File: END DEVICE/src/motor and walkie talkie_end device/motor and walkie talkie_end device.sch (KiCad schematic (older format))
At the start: 28 parts, among them J1 ICSP, J2 FTDI_CONN, SW1 SW_Push, SW2 SW_Push, SW3 SW_Push, SW4 SW_Push, SW5 SW_Push, U1 ATmega328P-MU, Y1 Crystal

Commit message: second commit: updated schematic symbol(oscillator)
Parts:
- Y1: value Crystal -> 8MHz
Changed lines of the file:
@@
 P 5200 2900
 F 0 "Y1" V 5154 3031 50  0000 L CNN
-F 1 "Crystal" V 5245 3031 50  0000 L CNN
+F 1 "8MHz" V 5245 3031 50  0000 L CNN
 F 2 "" H 5200 2900 50  0001 C CNN
 F 3 "~" H 5200 2900 50  0001 C CNN

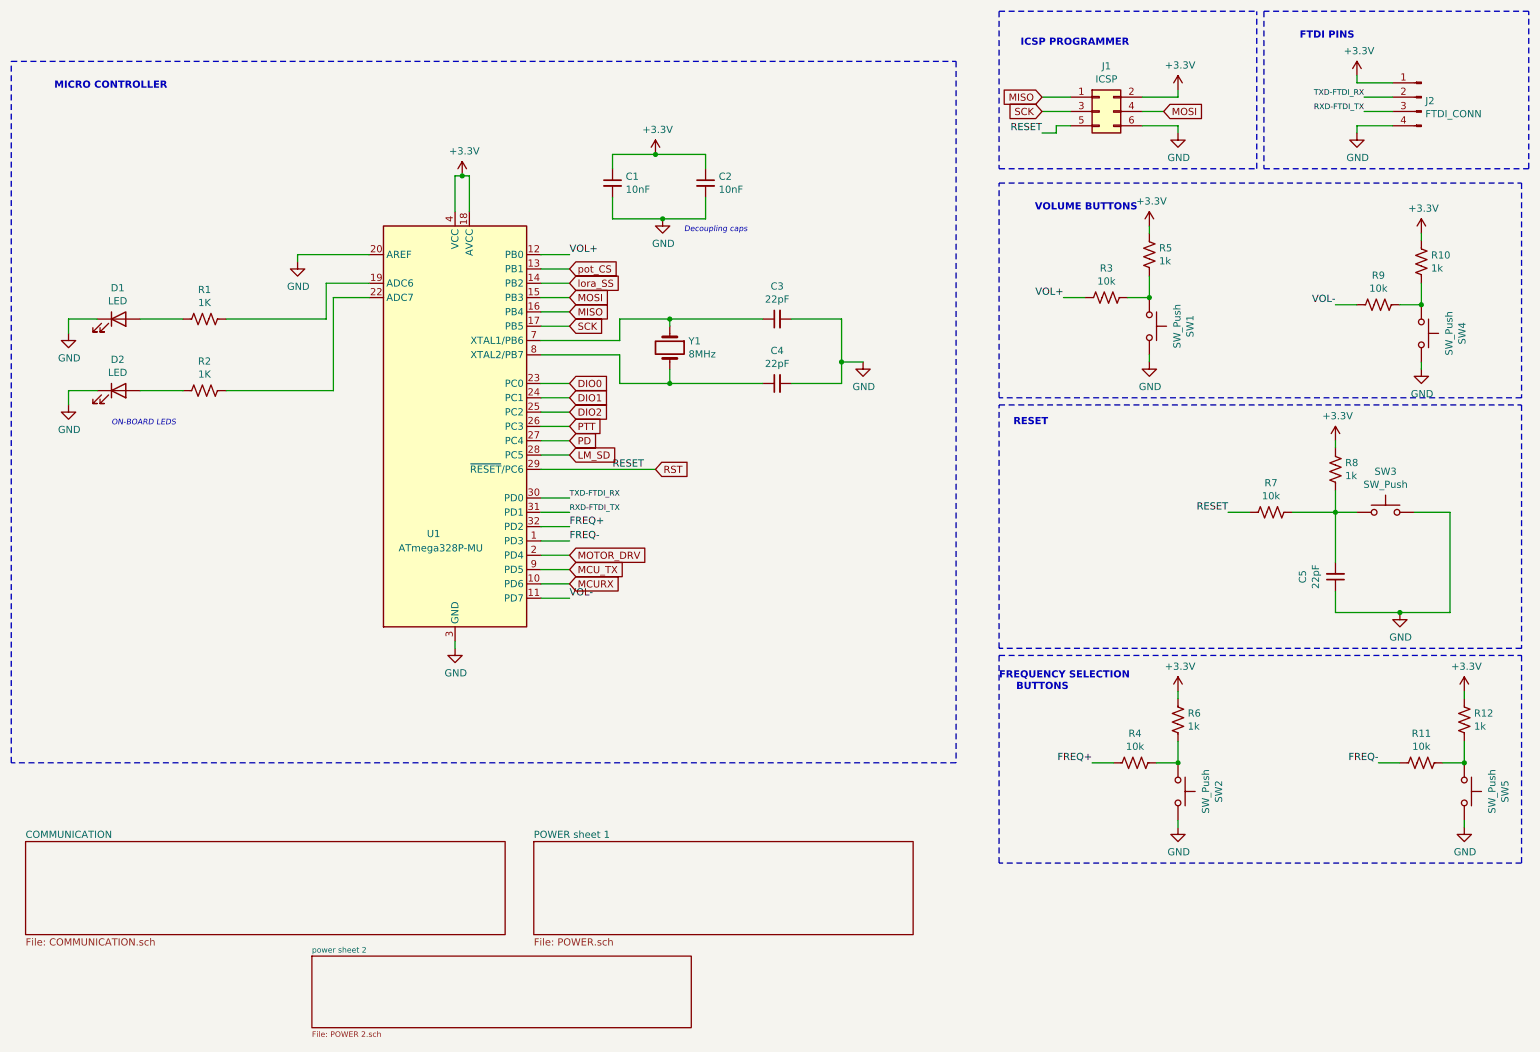
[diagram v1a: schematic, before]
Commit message: All footprint associations updated
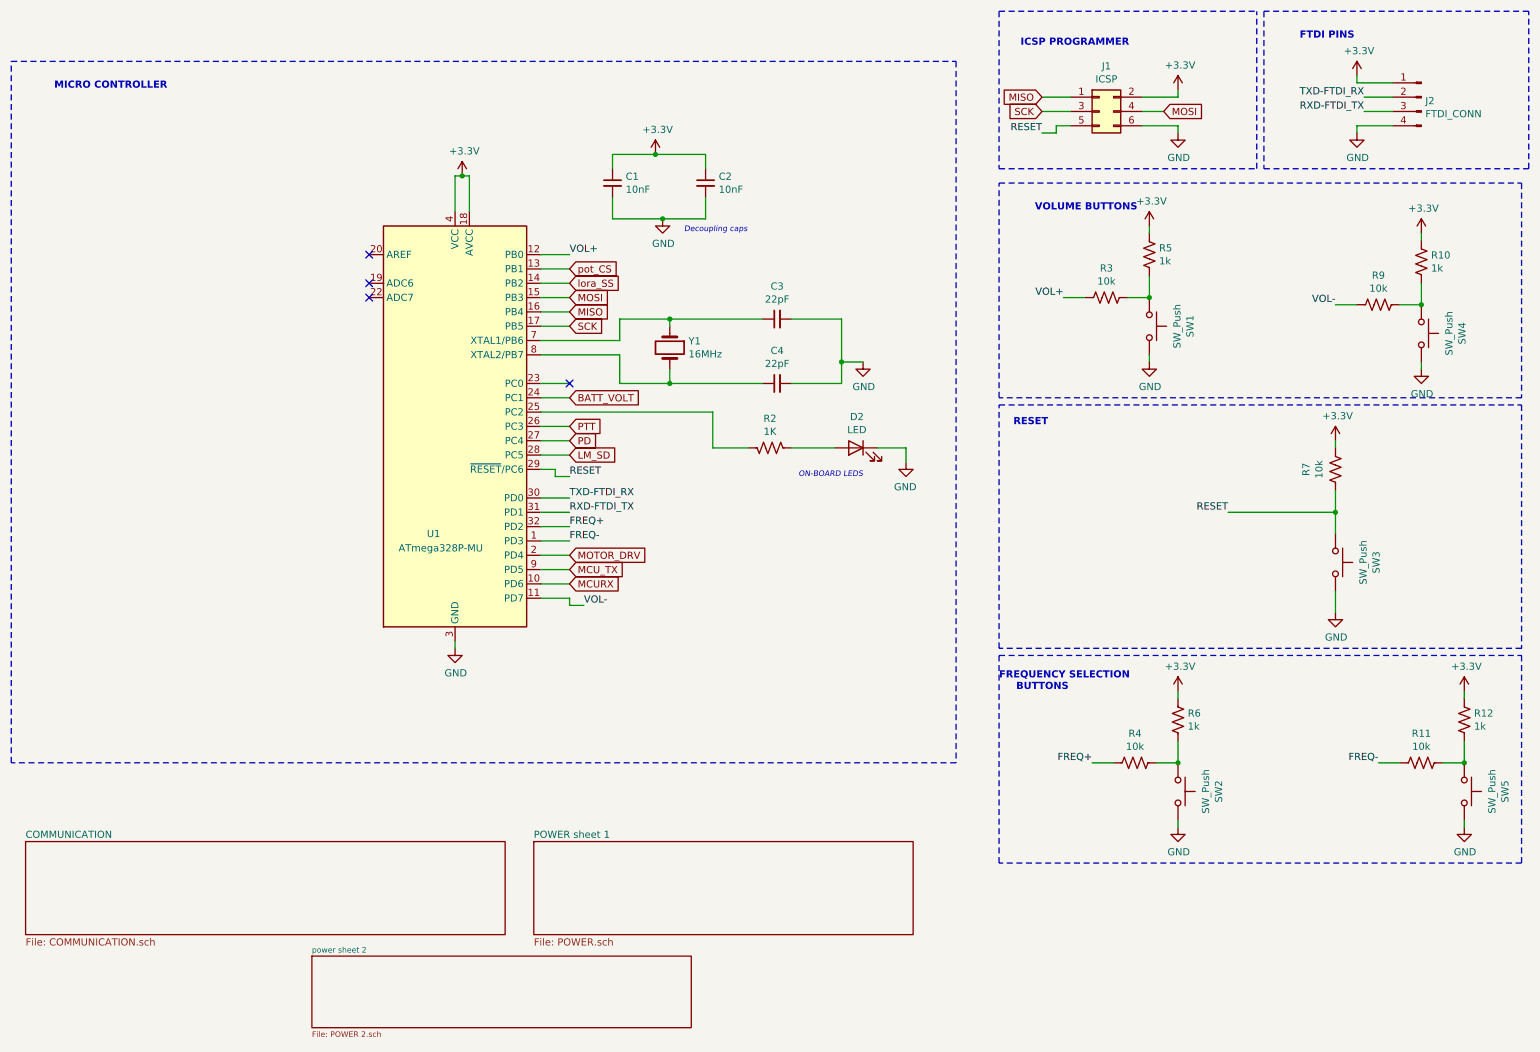
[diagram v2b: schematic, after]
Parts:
- removed C5: 22pF, symbol Device:C_Small
- removed D1: LED, symbol Device:LED
- removed R1: 1K, symbol Device:R_US
- removed R8: 1k, symbol Device:R_US
- C1, C2, C3, C4: footprint (none) -> Capacitor_SMD:C_0603_1608Metric
- D2: footprint (none) -> LED_SMD:LED_0603_1608Metric
- J1: footprint (none) -> Connector_PinHeader_2.54mm:PinHeader_2x03_P2.54mm_Vertical
- J2: footprint (none) -> Connector_PinHeader_2.54mm:PinHeader_1x04_P2.54mm_Vertical
- R10, R11, R12, R2, R3, R4, R5, R6, R7, R9: footprint (none) -> Resistor_SMD:R_0603_1608Metric
- SW1, SW2, SW3, SW4, SW5: footprint (none) -> Button_Switch_SMD:SW_SPST_B3U-1000P
- Y1: value 8MHz -> 16MHz; footprint (none) -> Crystal:Crystal_HC49-4H_Vertical
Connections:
- net RST is gone; now on net RESET: J1.5 (Pin_5), R7.1, U1.29 (~RESET~/PC6)
- net +3V3: now also R7.2
- net GND: no longer U1.20 (AREF)
- net at U1.22 (ADC7): no longer R2.1
- net RESET: now reaches SW3.1
- net RESET: no longer R7.2
- net DIO0: no longer names the net of U1.23 (PC0)
- net DIO1 renamed BATT_VOLT
- net DIO2: no longer names the net of U1.25 (PC2)
- net DIO2: now also R2.1
- no-connect marks 0 -> 4
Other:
- moved on the sheet: D2, R2, R7, SW3

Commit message: Project 99% complete and ready:Revision Needed
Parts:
- removed R10, R12, R5, R6: 1k, Resistor_SMD:R_0603_1608Metric, symbol Device:R_US
- added C16: 10nF, Capacitor_SMD:C_0603_1608Metric, symbol Device:C_Small
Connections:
- net +3V3: now also R11.1, R3.1, R4.1, R9.1, C16.1
- net FREQ+: now also R4.2, SW2.1; no longer R4.1
- net FREQ-: now also R11.2, SW5.1; no longer R11.1
- net GND: now also C16.2
- net VOL+: now also R3.2, SW1.1; no longer R3.1
- net VOL-: now also R9.2, SW4.1; no longer R9.1
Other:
- moved on the sheet: R11, R3, R4, R9
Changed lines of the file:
@@
 $EndComp
 Connection ~ 5100 1550
-Wire Wire Line
-	5100 1550 5450 1550
 $Comp
 L power:GND #PWR0103
@@
 $EndComp
 Wire Wire Line
-	8150 5800 8300 5800
-Wire Wire Line
 	8750 6200 8750 6250
 Wire Wire Line
@@
 	8750 5650 8750 5800
 Connection ~ 8750 5800
-Wire Wire Line
-	8600 5800 8750 5800
 $Comp
 L Switch:SW_Push SW2
@@
 L Device:R_US R4
 U 1 1 613770B0
-P 8450 5800
-F 0 "R4" V 8655 5800 50  0000 C CNN
-F 1 "10k" V 8564 5800 50  0000 C CNN
-F 2 "Resistor_SMD:R_0603_1608Metric" V 8490 5790 50  0001 C CNN
-F 3 "~" H 8450 5800 50  0001 C CNN
-	1    8450 5800
-	0    -1   -1   0
-$EndComp
-$Comp
-L Device:R_US R6
-U 1 1 613770BA
 P 8750 5500
-F 0 "R6" H 8818 5546 50  0000 L CNN
-F 1 "1k" H 8818 5455 50  0000 L CNN
+F 0 "R4" V 8955 5500 50  0000 C CNN
+F 1 "10k" V 8864 5500 50  0000 C CNN
 F 2 "Resistor_SMD:R_0603_1608Metric" V 8790 5490 50  0001 C CNN
 F 3 "~" H 8750 5500 50  0001 C CNN
@@
 $EndComp
 Wire Wire Line
-	9850 2600 10000 2600
-Wire Wire Line
 	10450 3000 10450 3050
 Wire Wire Line
@@
 	10450 2450 10450 2600
 Connection ~ 10450 2600
-Wire Wire Line
-	10300 2600 10450 2600
 $Comp
 L Switch:SW_Push SW4
@@
 L Device:R_US R9
 U 1 1 6137CA16
-P 10150 2600
-F 0 "R9" V 10355 2600 50  0000 C CNN
-F 1 "10k" V 10264 2600 50  0000 C CNN
-F 2 "Resistor_SMD:R_0603_1608Metric" V 10190 2590 50  0001 C CNN
-F 3 "~" H 10150 2600 50  0001 C CNN
-	1    10150 2600
-	0    -1   -1   0
-$EndComp
-$Comp
-L Device:R_US R10
-U 1 1 6137CA20
 P 10450 2300
-F 0 "R10" H 10518 2346 50  0000 L CNN
-F 1 "1k" H 10518 2255 50  0000 L CNN
+F 0 "R9" V 10655 2300 50  0000 C CNN
+F 1 "10k" V 10564 2300 50  0000 C CNN
 F 2 "Resistor_SMD:R_0603_1608Metric" V 10490 2290 50  0001 C CNN
 F 3 "~" H 10450 2300 50  0001 C CNN
@@
 $EndComp
 Wire Wire Line
-	7950 2550 8100 2550
-Wire Wire Line
 	8550 2950 8550 3000
 Wire Wire Line
@@
 	8550 2400 8550 2550
 Connection ~ 8550 2550
-Wire Wire Line
-	8400 2550 8550 2550
 $Comp
 L Switch:SW_Push SW1
@@
 L Device:R_US R3
 U 1 1 6138538C
-P 8250 2550
-F 0 "R3" V 8455 2550 50  0000 C CNN
-F 1 "10k" V 8364 2550 50  0000 C CNN
-F 2 "Resistor_SMD:R_0603_1608Metric" V 8290 2540 50  0001 C CNN
-F 3 "~" H 8250 2550 50  0001 C CNN
-	1    8250 2550
-	0    -1   -1   0
-$EndComp
-$Comp
-L Device:R_US R5
-U 1 1 61385396
 P 8550 2250
-F 0 "R5" H 8618 2296 50  0000 L CNN
-F 1 "1k" H 8618 2205 50  0000 L CNN
+F 0 "R3" V 8755 2250 50  0000 C CNN
+F 1 "10k" V 8664 2250 50  0000 C CNN
 F 2 "Resistor_SMD:R_0603_1608Metric" V 8590 2240 50  0001 C CNN
 F 3 "~" H 8550 2250 50  0001 C CNN
@@
 $EndComp
 $Comp
-L Device:R_US R12
-U 1 1 6136CBE7
+L Device:R_US R11
+U 1 1 6136CBDD
 P 10750 5500
-F 0 "R12" H 10818 5546 50  0000 L CNN
-F 1 "1k" H 10818 5455 50  0000 L CNN
+F 0 "R11" V 10955 5500 50  0000 C CNN
+F 1 "10k" V 10864 5500 50  0000 C CNN
 F 2 "Resistor_SMD:R_0603_1608Metric" V 10790 5490 50  0001 C CNN
 F 3 "~" H 10750 5500 50  0001 C CNN
 	1    10750 5500
 	1    0    0    -1
-$EndComp
-$Comp
-L Device:R_US R11
-U 1 1 6136CBDD
-P 10450 5800
-F 0 "R11" V 10655 5800 50  0000 C CNN
-F 1 "10k" V 10564 5800 50  0000 C CNN
-F 2 "Resistor_SMD:R_0603_1608Metric" V 10490 5790 50  0001 C CNN
-F 3 "~" H 10450 5800 50  0001 C CNN
-	1    10450 5800
-	0    -1   -1   0
 $EndComp
 $Comp
@@
 	0    1    1    0
 $EndComp
-Wire Wire Line
-	10600 5800 10750 5800
-Connection ~ 10750 5800
-Wire Wire Line
-	10750 5650 10750 5800
 $Comp
 L power:+3.3V #PWR0120
@@
 Wire Wire Line
 	10750 6200 10750 6250
-Wire Wire Line
-	10150 5800 10300 5800
 Wire Notes Line
 	7500 1650 9300 1650
@@
 	4400 3750 4300 3750
 NoConn ~ 3100 2250
+Wire Wire Line
+	7950 2550 8550 2550
+Wire Wire Line
+	9850 2600 10450 2600
+Wire Wire Line
+	8150 5800 8750 5800
+Wire Wire Line
+	10750 5650 10750 5800
+Connection ~ 10750 5800
+Wire Wire Line
+	10150 5800 10750 5800
+$Comp
+L Device:C_Small C16
+U 1 1 62A42084
+P 5950 1700
+F 0 "C16" H 6042 1746 50  0000 L CNN
+F 1 "10nF" H 6042 1655 50  0000 L CNN
+F 2 "Capacitor_SMD:C_0603_1608Metric" H 5950 1700 50  0001 C CNN
+F 3 "~" H 5950 1700 50  0001 C CNN
+	1    5950 1700
+	1    0    0    -1
+$EndComp
+Wire Wire Line
+	5950 1600 5950 1550
+Wire Wire Line
+	5100 1550 5450 1550
+Connection ~ 5450 1550
+Wire Wire Line
+	5450 1550 5950 1550
+Wire Wire Line
+	5450 2000 5950 2000
+Wire Wire Line
+	5950 1800 5950 2000
+Connection ~ 5450 2000
 $EndSCHEMATC

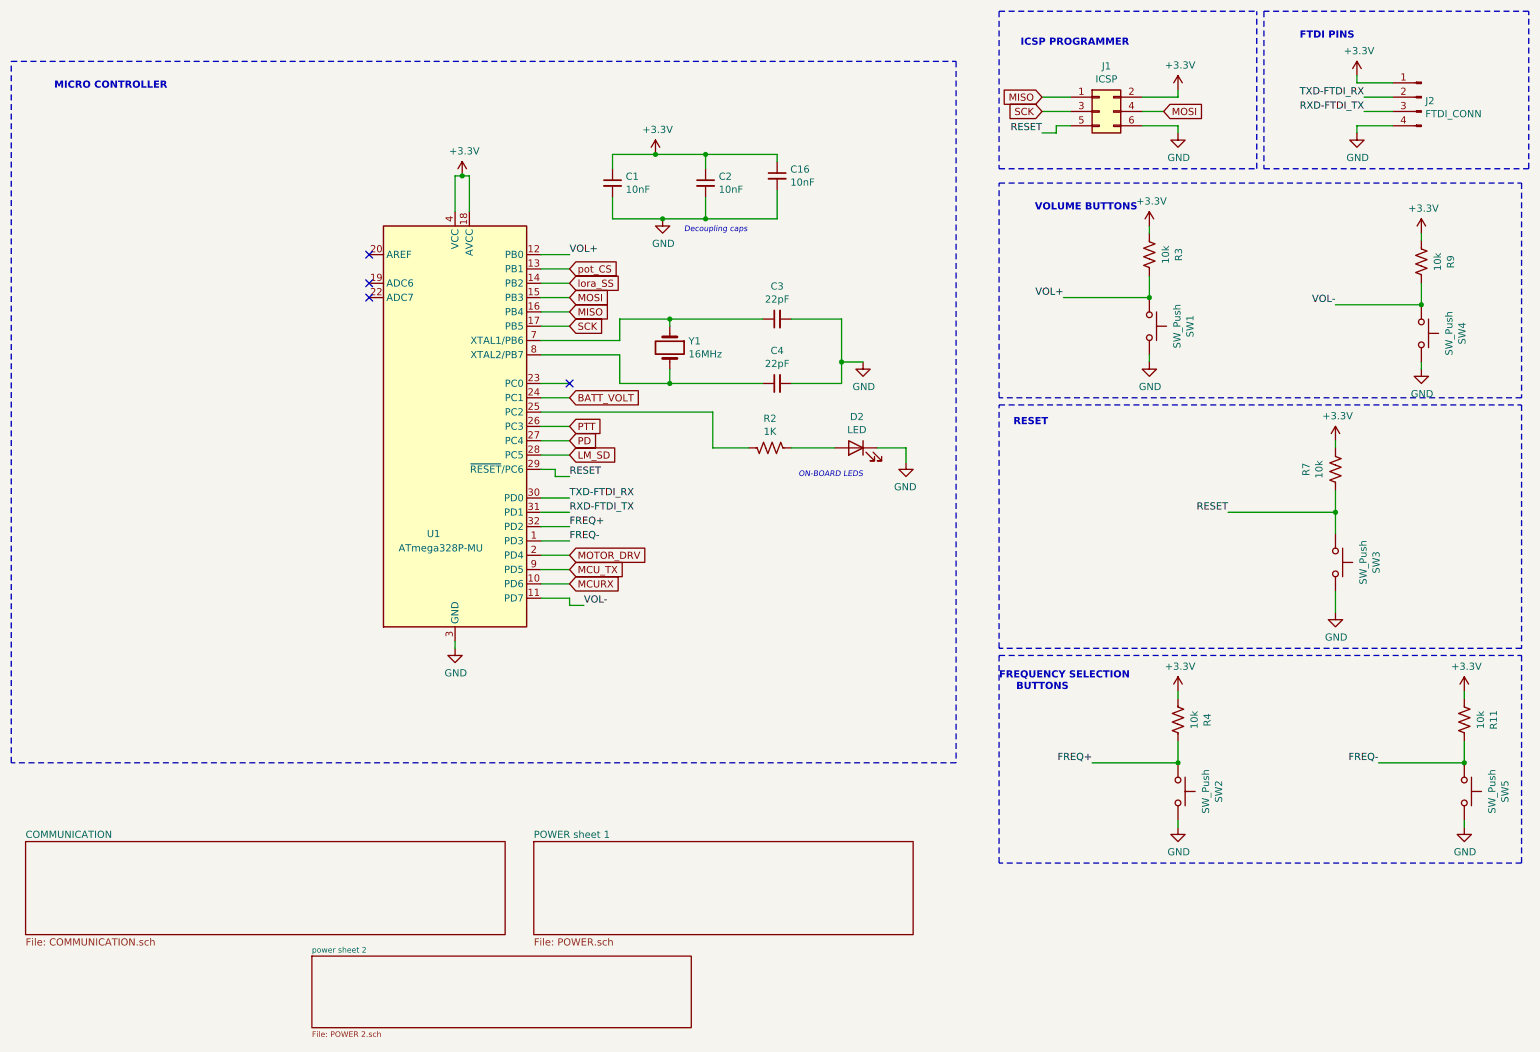
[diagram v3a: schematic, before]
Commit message: Version 2 compressed board
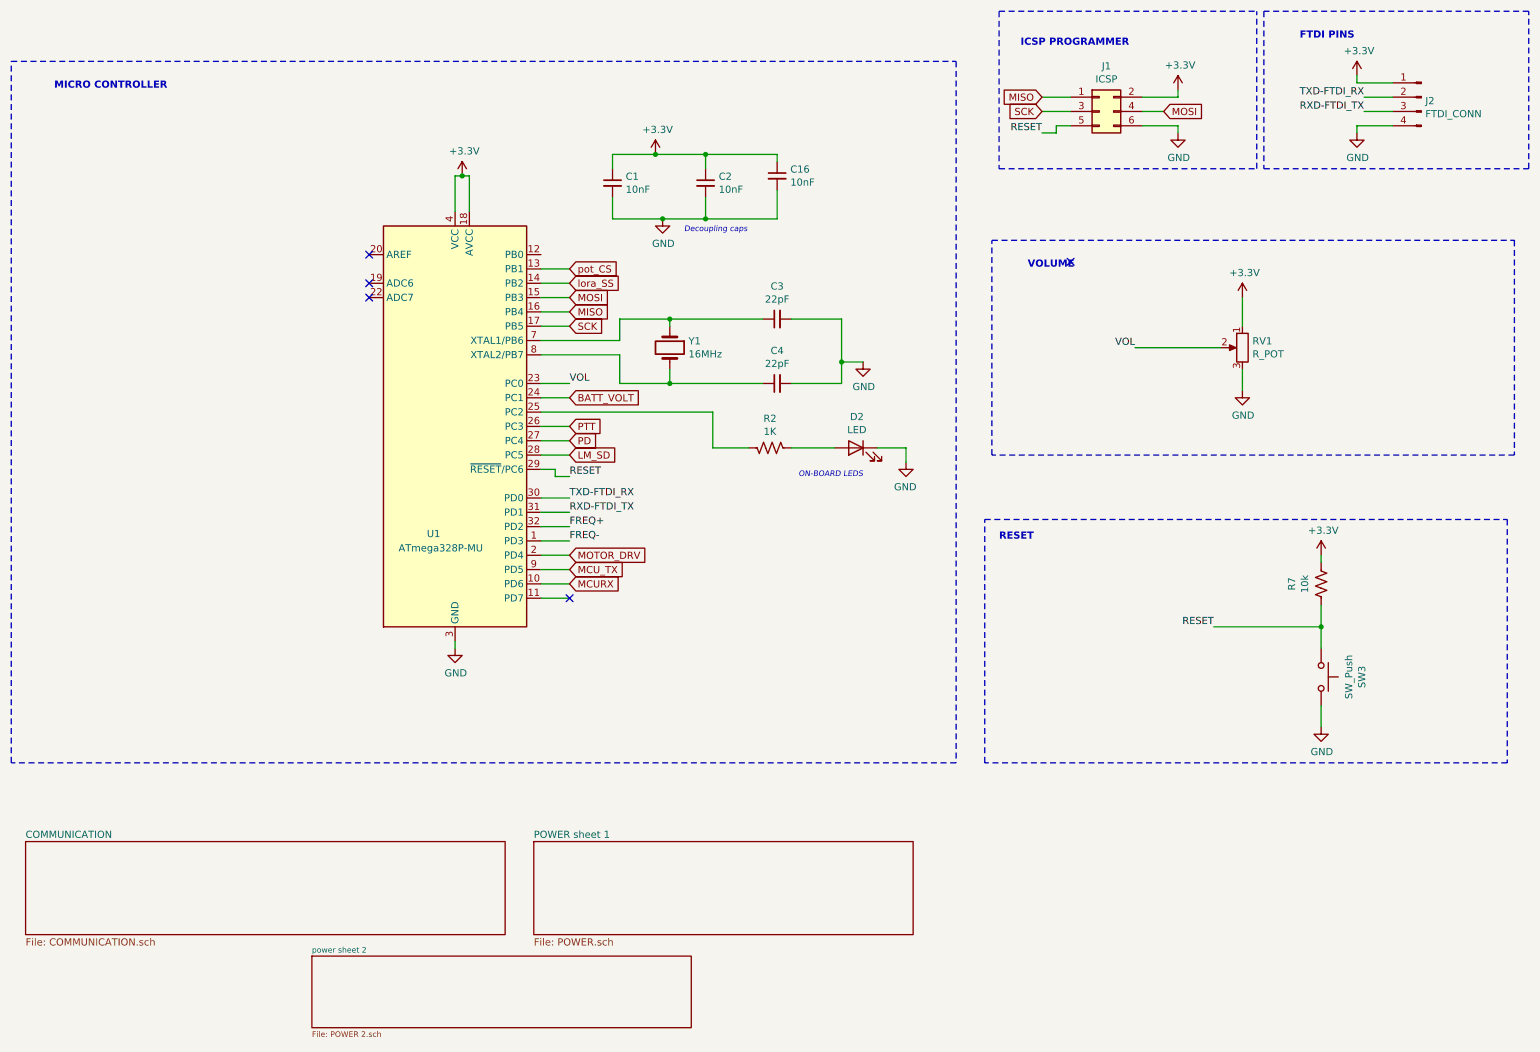
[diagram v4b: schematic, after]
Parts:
- removed R11, R3, R4, R9: 10k, Resistor_SMD:R_0603_1608Metric, symbol Device:R_US
- removed SW1, SW2, SW4, SW5: SW_Push, Button_Switch_SMD:SW_SPST_B3U-1000P, symbol Switch:SW_Push
- added RV1: R_POT, Potentiometer_THT:Potentiometer_Alps_RK163_Single_Horizontal, symbol Device:R_POT
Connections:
- net +3V3: now also RV1.1
- net GND: now also RV1.3
- net VOL: now reaches U1.23 (PC0)
- net VOL: now also RV1.2
- net VOL+: no longer names the net of U1.12 (PB0)
- net VOL-: no longer names the net of U1.11 (PD7)
- no-connect marks 4 -> 5
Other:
- note added: "VOLUME"
- note removed: "FREQUENCY SELECTION\n BUTTONS"
- note removed: "VOLUME BUTTONS"
- moved on the sheet: R7, SW3

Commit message: latest update
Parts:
- RV1: footprint Potentiometer_THT:Potentiometer_Alps_RK163_Single_Horizontal -> Potentiometer_THT:Potentiometer_Piher_PC-16_Single_Horizontal
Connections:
- net FREQ- is gone; now on net MOTOR_DRV: U1.1 (PD3)
- net MOTOR_DRV: no longer U1.2 (PD4)
- net FREQ+: no longer names the net of U1.32 (PD2)
- no-connect marks 5 -> 8
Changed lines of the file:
@@
 Text Label 4500 3150 0    50   ~ 0
 VOL
-Text Label 4500 4150 0    50   ~ 0
-FREQ+
-Text Label 4500 4250 0    50   ~ 0
-FREQ-
 Wire Wire Line
 	4500 3950 4300 3950
@@
 Wire Wire Line
 	4500 4550 4300 4550
-Text GLabel 4500 4350 2    50   Input ~ 0
-MOTOR_DRV
 Wire Wire Line
 	4500 4350 4300 4350
@@
 F 0 "RV1" H 9130 2946 50  0000 R CNN
 F 1 "R_POT" H 9130 2855 50  0000 R CNN
-F 2 "Potentiometer_THT:Potentiometer_Alps_RK163_Single_Horizontal" H 9200 2900 50  0001 C CNN
+F 2 "Potentiometer_THT:Potentiometer_Piher_PC-16_Single_Horizontal" H 9200 2900 50  0001 C CNN
 F 3 "~" H 9200 2900 50  0001 C CNN
 	1    9200 2900
@@
 Wire Wire Line
 	9200 2550 9200 2750
+NoConn ~ 4500 4350
+NoConn ~ 8000 2300
+Text GLabel 4500 4250 2    50   Input ~ 0
+MOTOR_DRV
+NoConn ~ 4500 4150
 NoConn ~ 4500 4650
-NoConn ~ 8000 2300
+NoConn ~ 4300 2250
 $EndSCHEMATC

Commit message: Everythinhg is set
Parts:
- removed Y1: 16MHz, Crystal:Crystal_HC49-4H_Vertical, symbol Device:Crystal
- added Y1: 16MHz, Crystal:Crystal_SMD_Abracon_ABM8G-4Pin_3.2x2.5mm, symbol Device:Crystal_GND24
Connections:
- net at C3.1, U1.7 (XTAL1/PB6): now also Y1.3
- net at C4.1, U1.8 (XTAL2/PB7): now also Y1.1
- no-connect marks 8 -> 10
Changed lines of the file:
@@
 	3700 5000 3700 4950
-$Comp
-L Device:Crystal Y1
-U 1 1 6133D1C8
-P 5200 2900
-F 0 "Y1" V 5154 3031 50  0000 L CNN
-F 1 "16MHz" V 5245 3031 50  0000 L CNN
-F 2 "Crystal:Crystal_HC49-4H_Vertical" H 5200 2900 50  0001 C CNN
-F 3 "~" H 5200 2900 50  0001 C CNN
-	1    5200 2900
-	0    1    1    0
-$EndComp
 $Comp
 L Device:C_Small C3
@@
 Wire Wire Line
 	5200 3050 5200 3150
-Wire Wire Line
-	5200 3150 5850 3150
 Wire Wire Line
 	6050 3150 6400 3150
@@
 NoConn ~ 4500 4650
 NoConn ~ 4300 2250
+$Comp
+L Device:Crystal_GND24 Y1
+U 1 1 614C86C4
+P 5200 2900
+F 0 "Y1" V 5246 2656 50  0000 R CNN
+F 1 "16MHz" V 5155 2656 50  0000 R CNN
+F 2 "Crystal:Crystal_SMD_Abracon_ABM8G-4Pin_3.2x2.5mm" H 5200 2900 50  0001 C CNN
+F 3 "~" H 5200 2900 50  0001 C CNN
+	1    5200 2900
+	0    -1   -1   0
+$EndComp
+Wire Wire Line
+	5200 3150 5850 3150
+NoConn ~ 5000 2900
+NoConn ~ 5400 2900
 $EndSCHEMATC
